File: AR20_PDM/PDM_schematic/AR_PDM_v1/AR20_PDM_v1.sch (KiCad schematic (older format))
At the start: 14 parts, among them J1 High_Curret_terminal, J2 1-776163-1, U1 ACM_2020

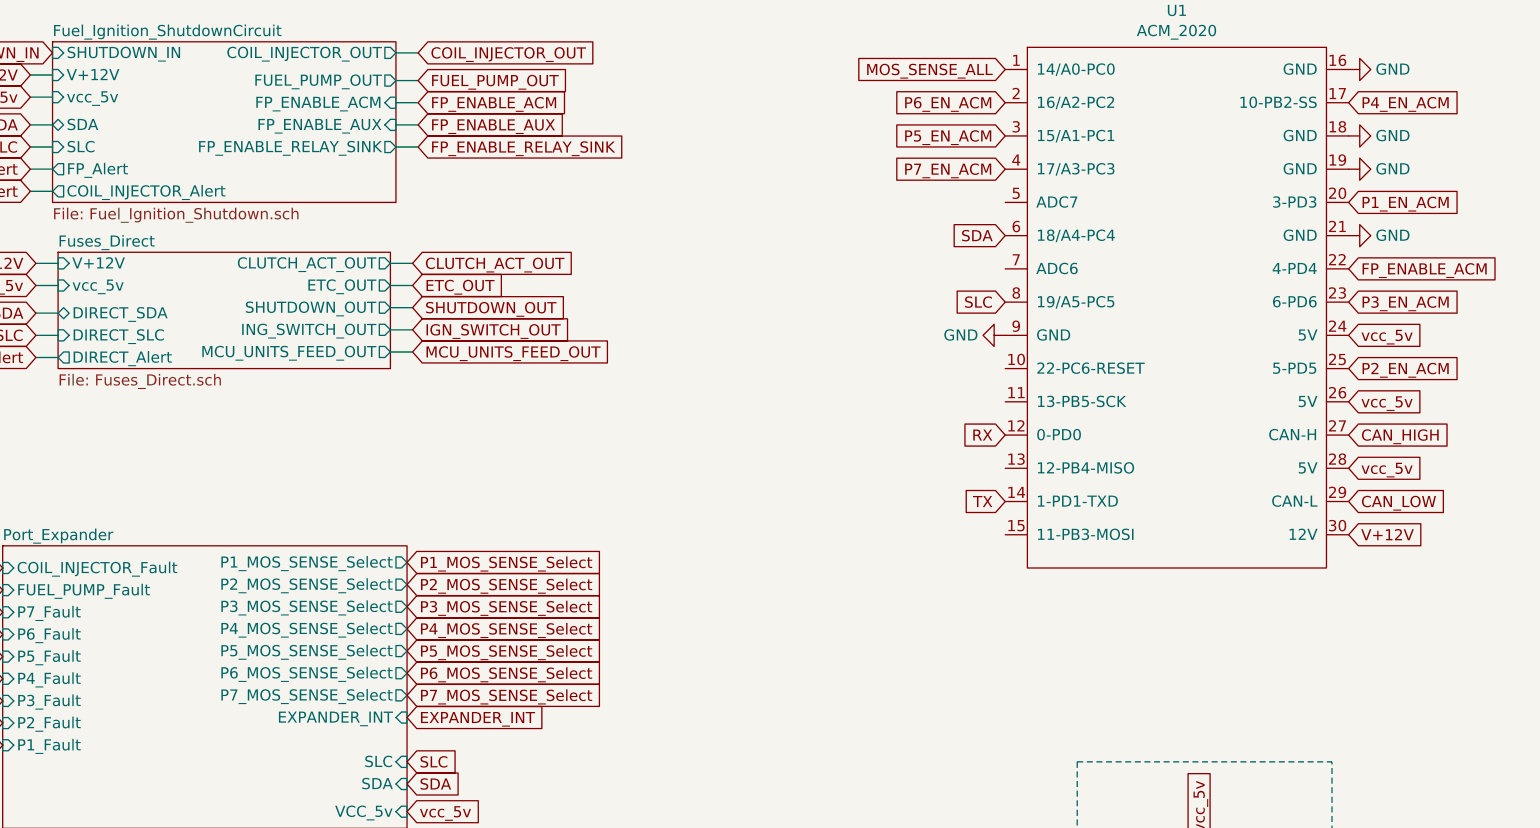
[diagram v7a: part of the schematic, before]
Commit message: PCB design, and misc, see description, work in progress
- added shutdown circuit for ACM shutdown capability
PCB layout, in progress: 
- added copper pour for 12 volt, for fuses
- arranged indicator LED's
- arranged some of the P1-P7 caps and resistors
- re arranged P1-p7 in ascending order.
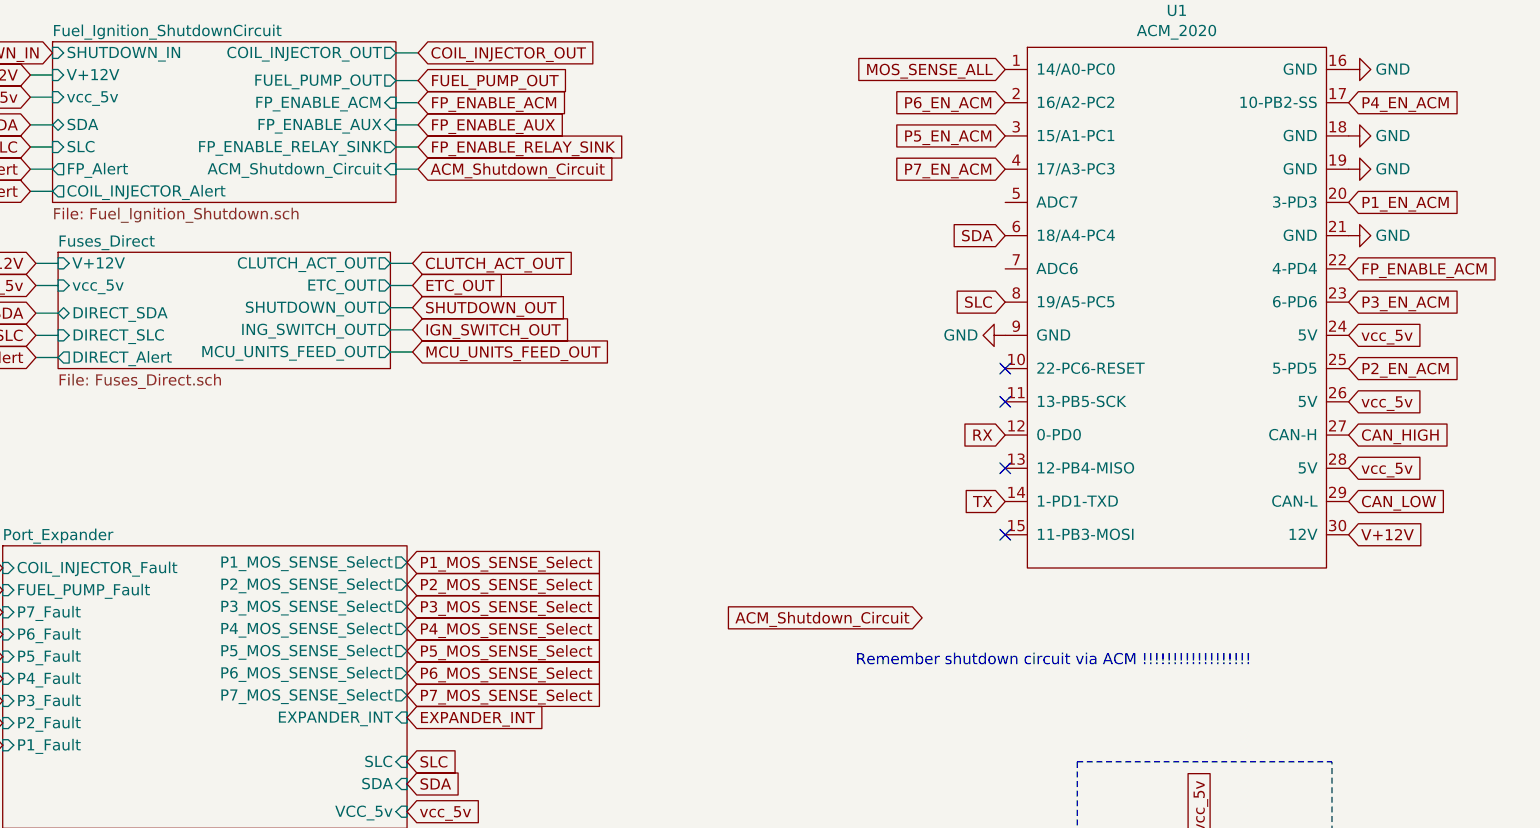
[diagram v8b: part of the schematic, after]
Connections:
- no-connect marks 0 -> 4
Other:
- note added: "Remember shutdown circuit via ACM !!!!!!!!!!!!!!!!!!"
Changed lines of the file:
@@
 F12 "FP_ENABLE_AUX" I R 10000 1075 50
 F13 "FP_ENABLE_RELAY_SINK" O R 10000 1175 50
+F14 "ACM_Shutdown_Circuit" I R 10000 1275 50
 $EndSheet
 $Sheet
@@
 Wire Wire Line
 	2125 4850 2225 4850
+Text Notes 12075 3525 0    50   ~ 0
+Remember shutdown circuit via ACM !!!!!!!!!!!!!!!!!!
+Text GLabel 10100 1275 2    50   Input ~ 0
+ACM_Shutdown_Circuit
+Wire Wire Line
+	10100 1275 10000 1275
+Text GLabel 12375 3300 0    50   Input ~ 0
+ACM_Shutdown_Circuit
+NoConn ~ 12750 2325
+NoConn ~ 12750 2175
+NoConn ~ 12750 2625
+NoConn ~ 12750 2925
 $EndSCHEMATC
